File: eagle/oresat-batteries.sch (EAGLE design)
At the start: 101 parts, among them IC1 74AHC1G08DBV, J6 J-SAMTEC-TFM-120-X1-XXX-D-RA, J7 1.27MM-SWD-CONNECTOR, Q1 CSD16340Q3, Q2 CSD16340Q3, Q3 TPN4R712MD, Q4 TPN4R712MD, Q5 TPN4R712MD, Q6 TPN4R712MD, Q7 CSD16340Q3, U1 TPS63070, U10 LTC4412, U11 MAX17055, U12 LTC4412, U13 LTC4412, U2 TCAN330, U3 BQ2970, U4 LTC4411, U5 LTC4411, U6 STM32F042K6, U7 LTC4411, U8 LTC4411, U9 LTC4412, X1 16MHZ-2.5x2mm

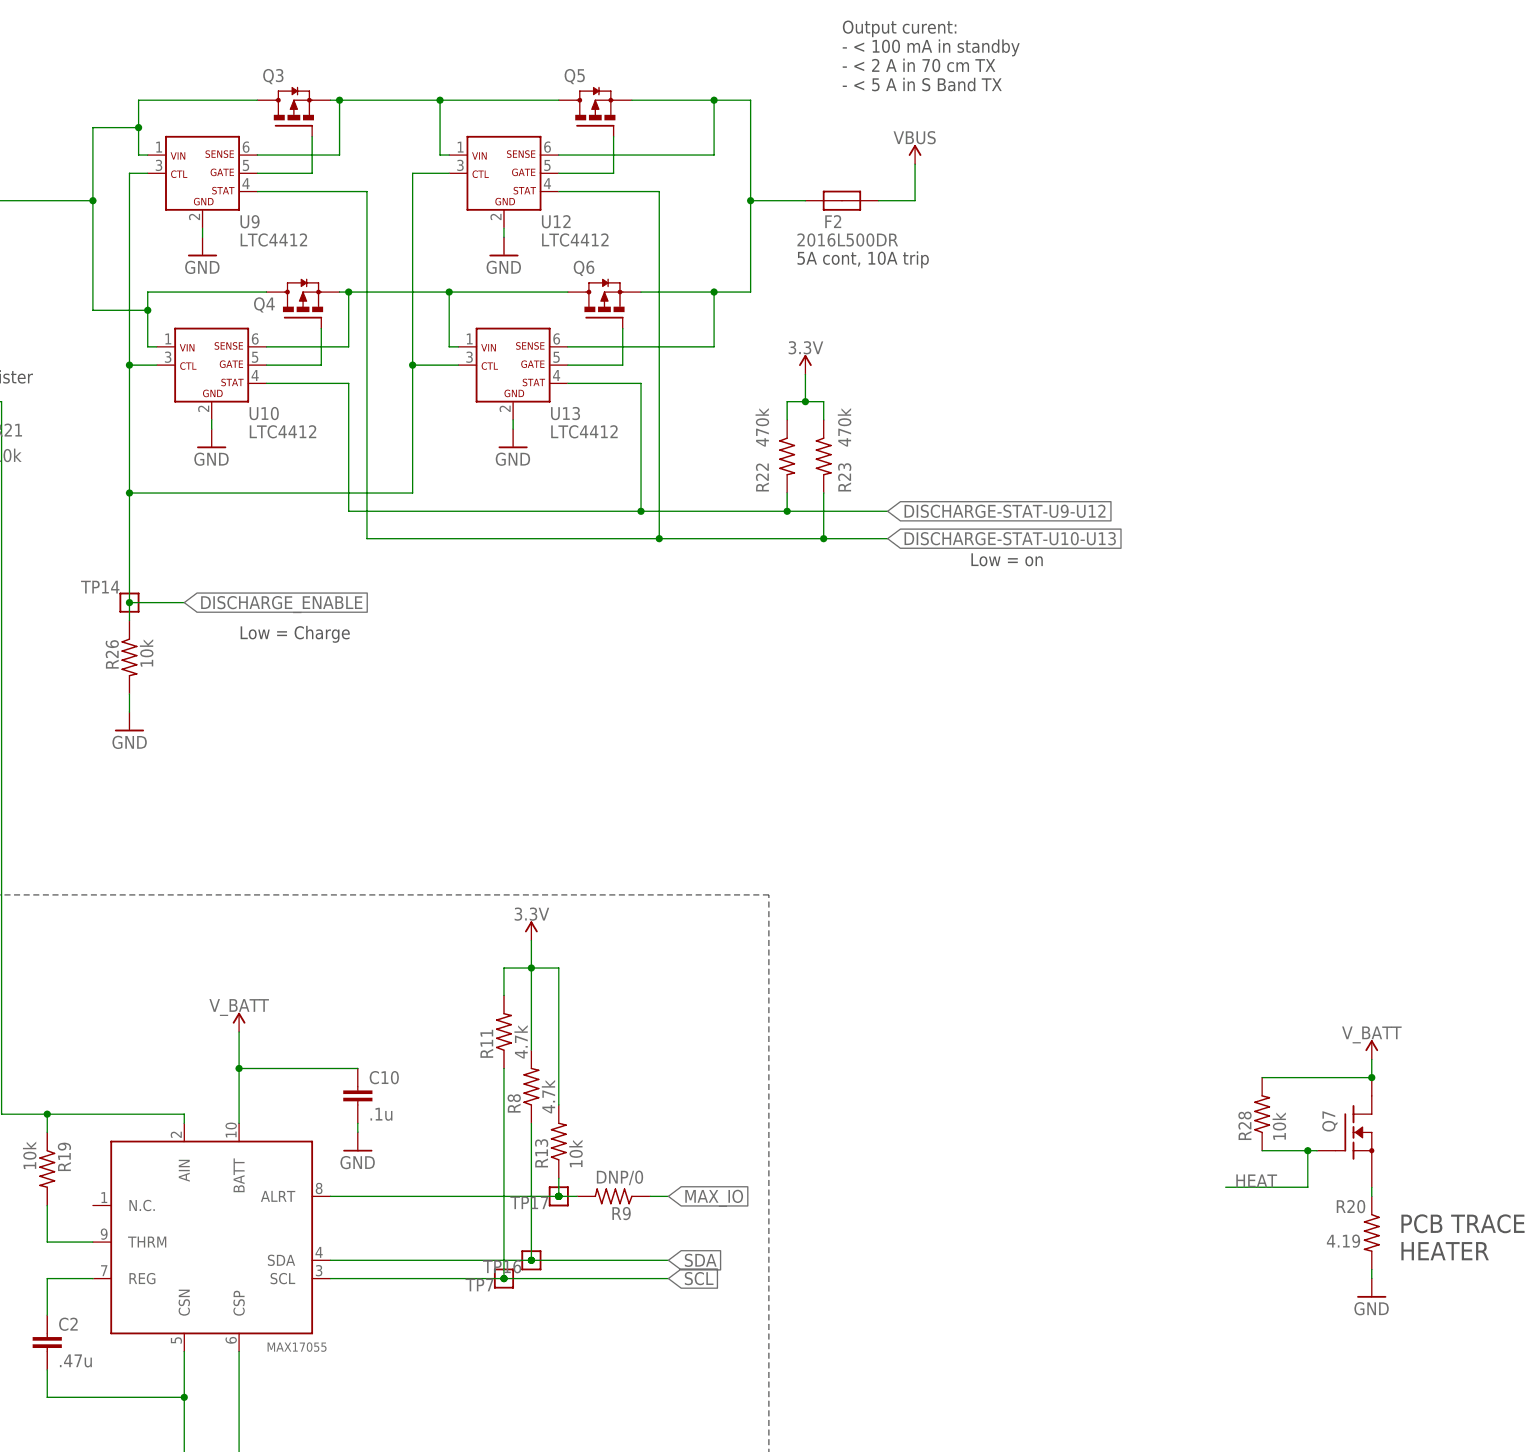
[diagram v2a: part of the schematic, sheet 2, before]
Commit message: Fixed body diode issue on output.  Changed N to P mosfett for 'trace heater.'
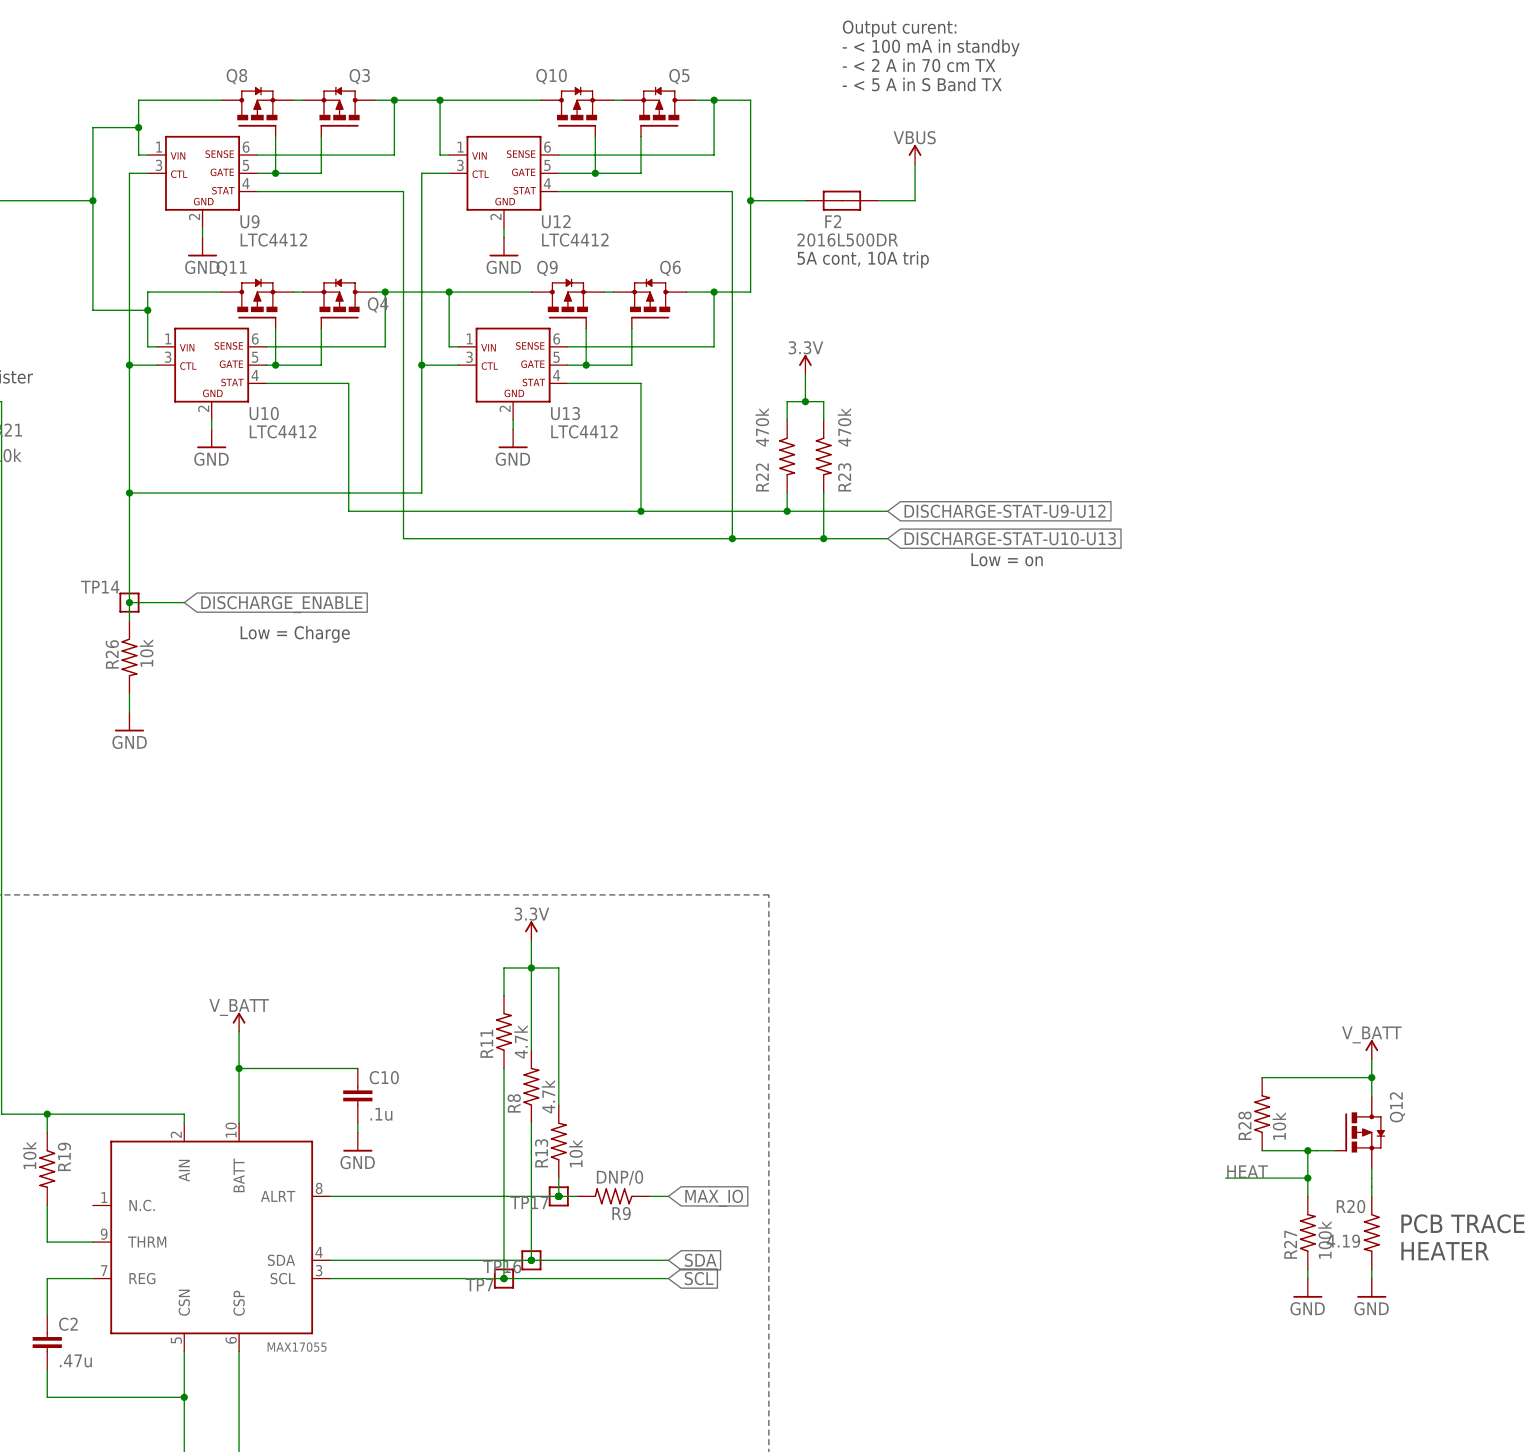
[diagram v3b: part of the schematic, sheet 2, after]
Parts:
- removed Q7: CSD16340Q3, oresat-batteries:CSD16340Q3
- added Q10, Q11, Q12, Q8, Q9: TPN4R712MD, tpn4r712md-pmosfet:TPN4R712MD
- added R27: 100k, rcl:R-US_R0603
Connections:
- removed net N$440: Q4.S, Q6.D, U10.SENSE, U13.VIN
- new net .3556: Q4.D, Q9.D, U10.SENSE, U13.VIN
- new net N$2: Q3.S, Q8.S
- new net N$3: Q10.S, Q5.S
- new net N$4: Q11.S, Q4.S
- new net N$5: Q6.S, Q9.S
- net GND: now also R27.1
- net HEAT: now also Q12.G, R27.2; no longer Q7.G
- net N$435: now also Q12.S; no longer Q7.S
- net N$436: now also Q10.G
- net N$437: now also Q10.D, Q3.D; no longer Q3.S, Q5.D
- net N$438: now also Q8.G
- net N$439: now also Q9.G
- net N$441: now also Q11.G
- net OUTFUSE: now also Q5.D, Q6.D; no longer Q5.S, Q6.S
- net V_BATT: now also Q11.D, Q12.D, Q8.D; no longer Q3.D, Q4.D, Q7.D
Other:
- note removed: "CHANGE ME: CHANGE TO P CHANNEL"
- moved on the sheet: Q3, Q4, Q5, Q6

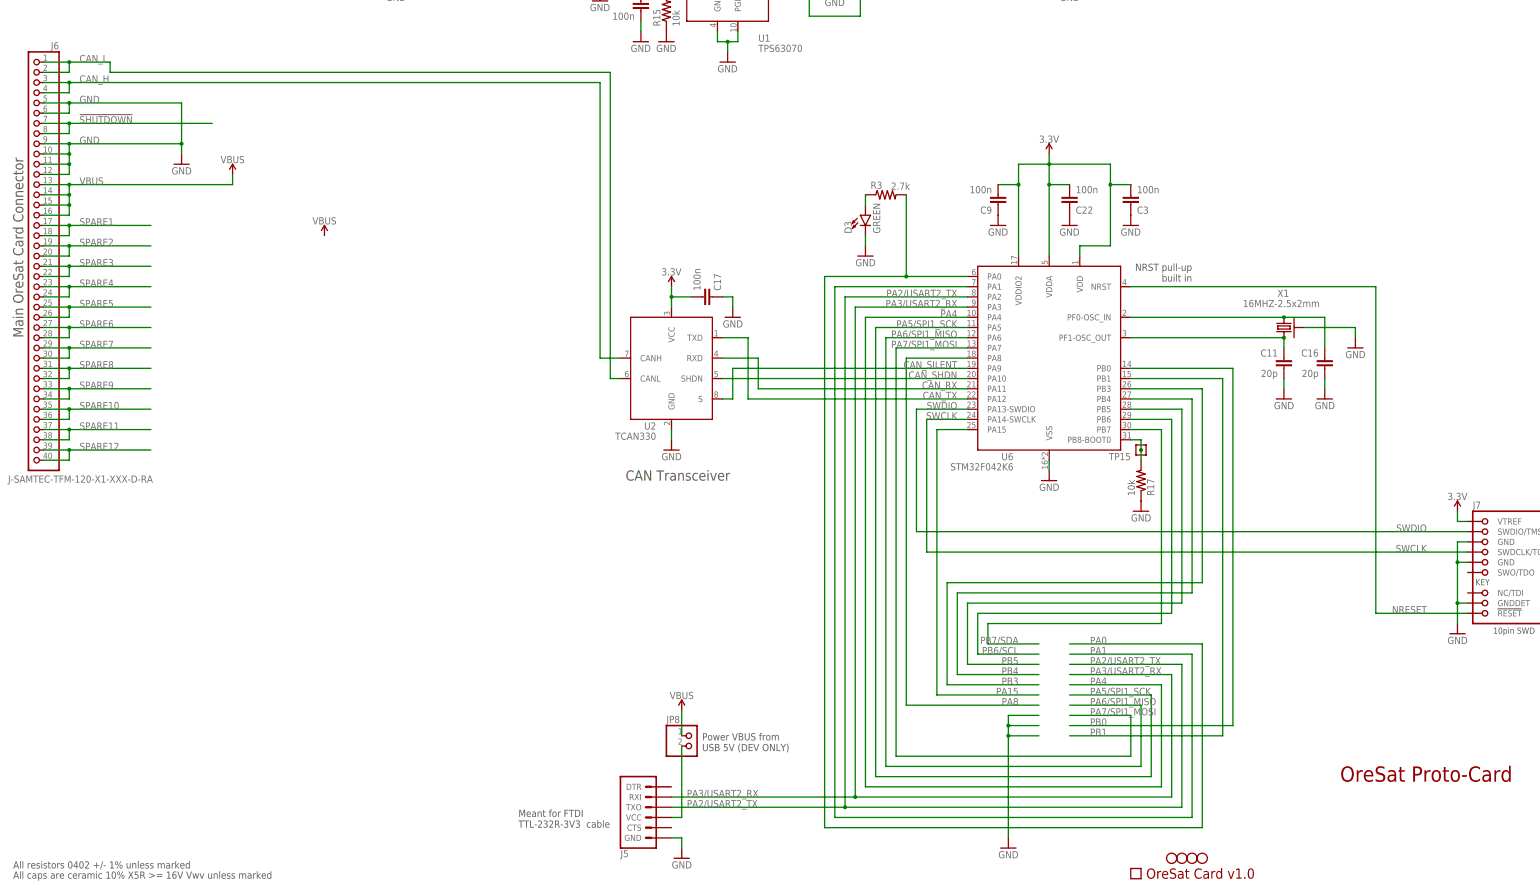
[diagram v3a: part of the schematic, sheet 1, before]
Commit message: Assigned IO pins to circuit functions.  Finished controls for heater.
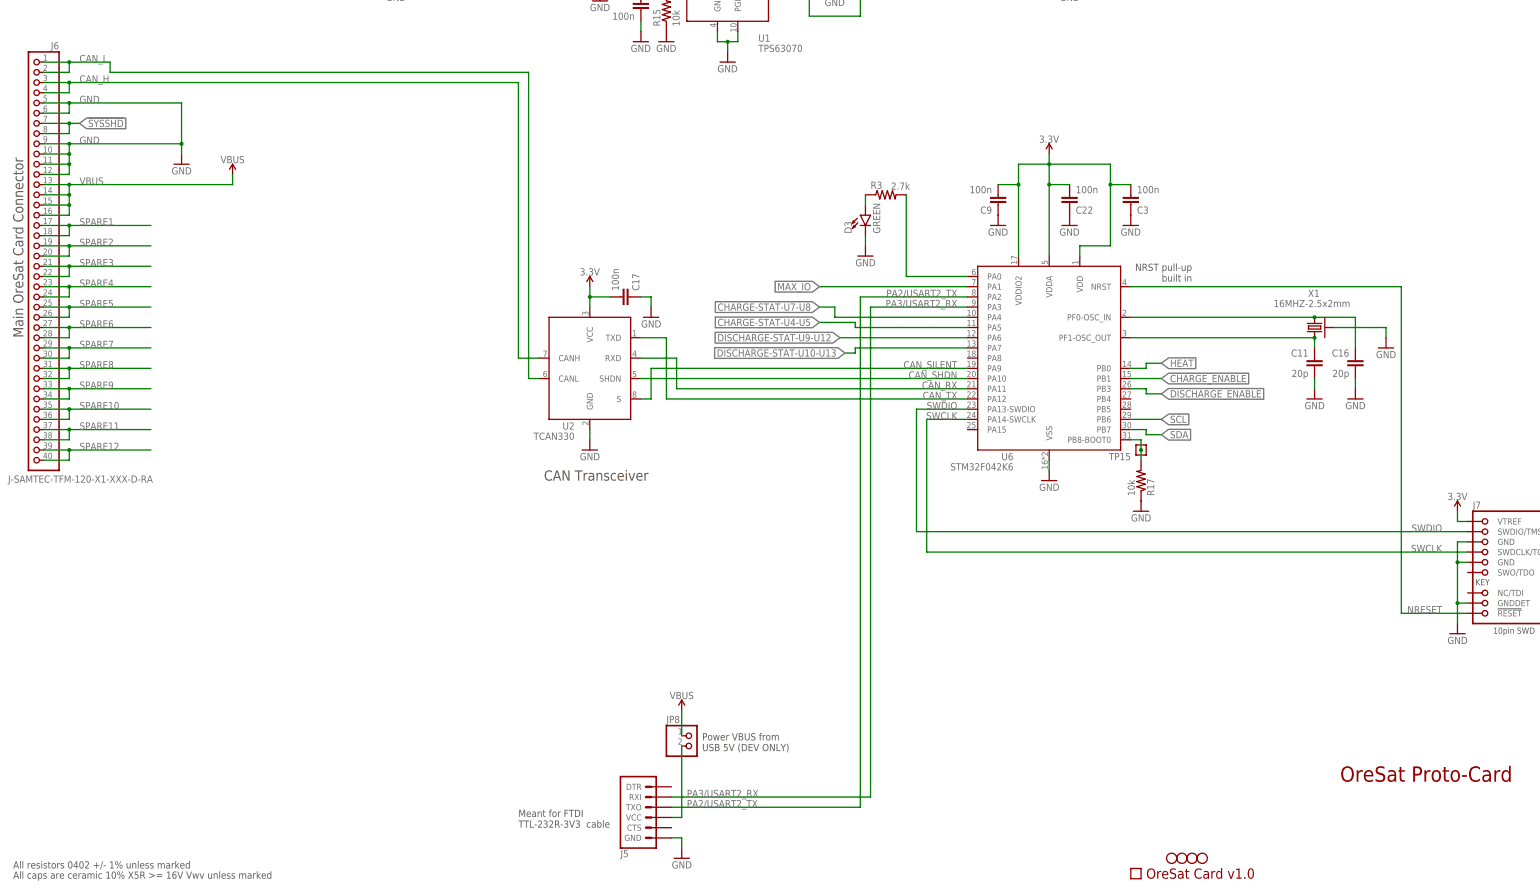
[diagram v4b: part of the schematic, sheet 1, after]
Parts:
- added U$1: MMBT3904-TP, mmbt3904-tp:MMBT3904-TP
- R27: value 100k -> 3.3k; device rcl:R-US_R0603 -> rcl:R-US_R0402
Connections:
- removed net !SHUTDOWN: J6.7, J6.8
- removed net N$435: Q12.S, R20.1
- removed net PA1: U6.PA1
- removed net PA15: U6.PA15
- removed net PA4: U6.PA4
- removed net PA5/SPI1_SCK: U6.PA5
- removed net PA6/SPI1_MISO: U6.PA6
- removed net PA7/SPI1_MOSI: U6.PA7
- removed net PA8: U6.PA8
- removed net PB0: U6.PB0
- removed net PB1: U6.PB1
- removed net PB3: U6.PB3
- removed net PB4: U6.PB4
- removed net PB5: U6.PB5
- removed net PB6/SCL: U6.PB6
- removed net PB7/SDA: U6.PB7
- removed net SYSSHD: IC1A.I0, R14.2, TP8.P$1
- new net !SYSSHD: IC1A.I0, J6.7, J6.8, R14.2, TP8.P$1
- new net HEAT_FET_CTL: Q12.G, R28.1, U$1.C
- new net N$6: Q12.D, R20.1
- new net N$7: R27.2, U$1.B
- net CHARGE-STAT-U4-U5: now also U6.PA5
- net CHARGE-STAT-U7-U8: now also U6.PA4
- net CHARGE_ENABLE: now also U6.PB1
- net DISCHARGE-STAT-U10-U13: now also U6.PA7
- net DISCHARGE-STAT-U9-U12: now also U6.PA6
- net DISCHARGE_ENABLE: now also U6.PB3
- net GND: now also U$1.E; no longer R27.1
- net HEAT: now also R27.1, U6.PB0; no longer Q12.G, R27.2, R28.1
- net MAX_IO: now also U6.PA1
- net SCL: now also U6.PB6
- net SDA: now also U6.PB7
- net V_BATT: now also Q12.S; no longer Q12.D
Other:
- note added: "-3.9V"
- note added: "Low = Discharge"
- note removed: "CHECK BODY DIODES"
- note removed: "HEAT"
- moved on the sheet: C11, C16, C17, Q12, R27, R28, U2, X1

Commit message: Last changes to previous 1 cell battery pack. Abandoning for 2 cell packs because we're weenies.
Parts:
- removed CARD: ORESAT-CARD-V0.5, oresat-card:ORESAT-CARD-V0.5
- J1: DIS Digi-Key -> (none); DPN SAM10145-ND -> (none); MFR Samtec -> (none); MPN TFM-120-01-L-D-RA -> (none)
- renumbered J6 to J1
